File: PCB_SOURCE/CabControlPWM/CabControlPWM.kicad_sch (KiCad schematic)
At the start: 20 parts, among them J102 Jack-DC

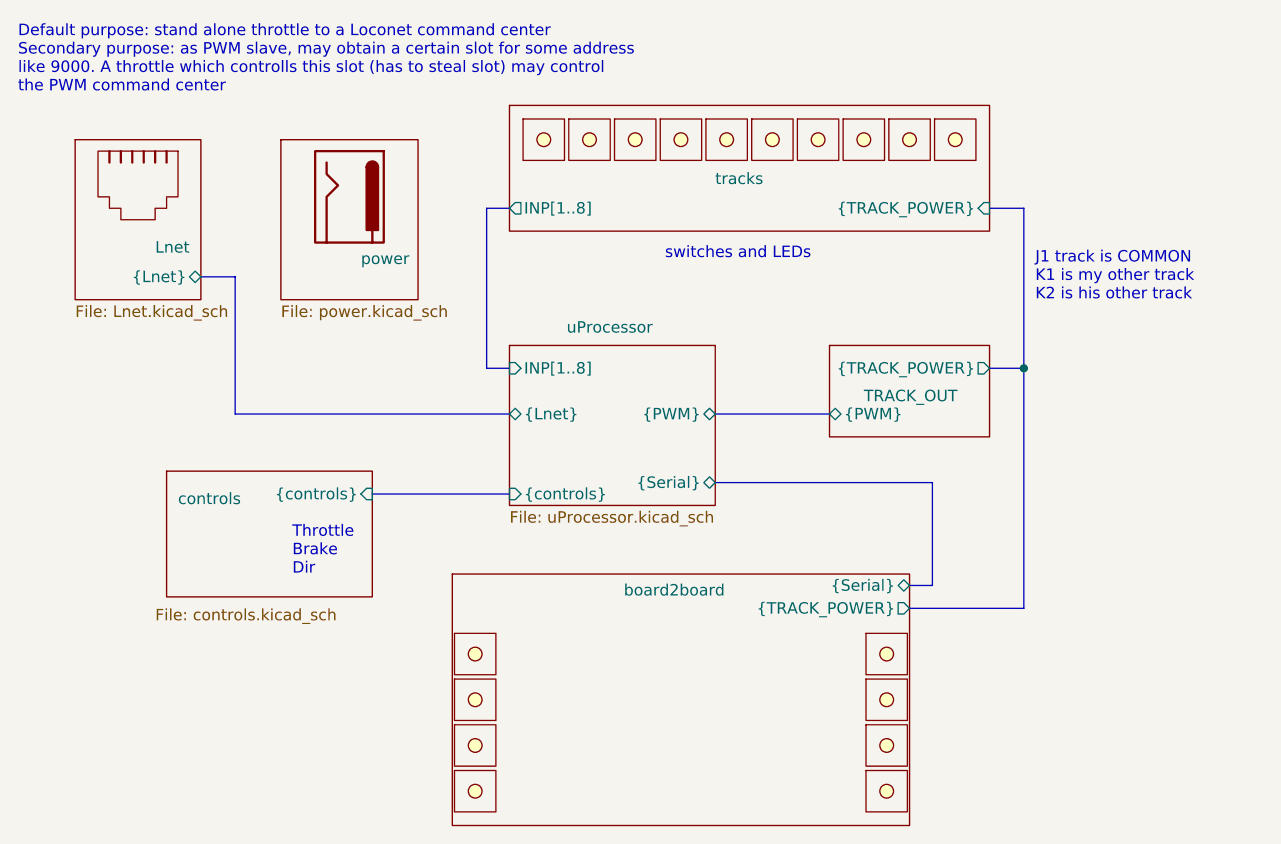
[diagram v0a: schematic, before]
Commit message: fixed bug in ahob program among others
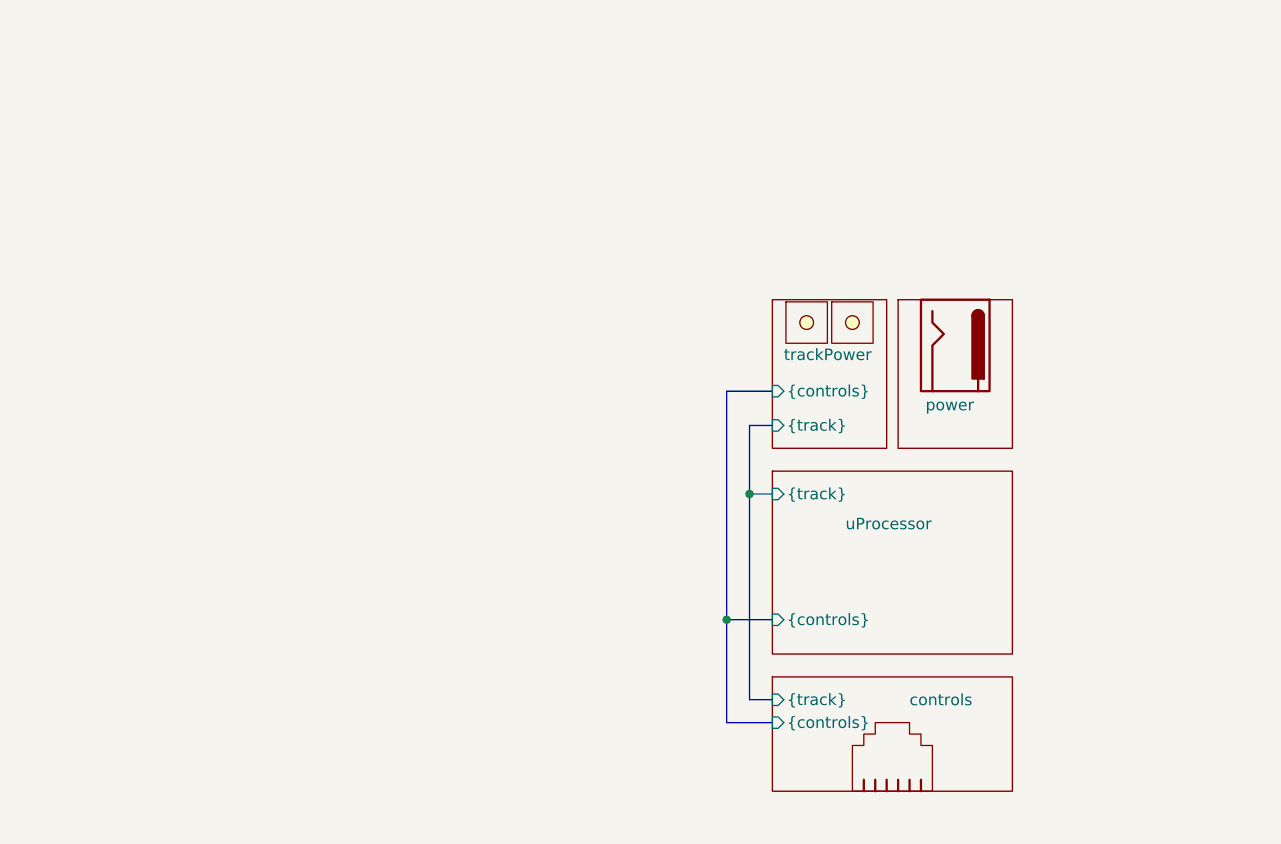
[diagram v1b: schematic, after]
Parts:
- removed u103, u104, u105, u106, u107, u108, u109, u110, u111, u112, u113, u114, u115, u116, u117, u118: ~, symbol custom_kicad_lib_sk:screwterminal
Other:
- removed sheet Lnet
- removed sheet TRACK_OUT
- removed sheet board2board
- removed sheet tracks
- added sheet trackPower (trackPower.kicad_sch)
- sheet controls ports: added {track}; removed none
- sheet uProcessor: file uProcessor.kicad_sch -> attiny85.kicad_sch
- sheet uProcessor ports: added {track}; removed INP[1..8], {Lnet}, {PWM}, {Serial}
- note removed: "Default purpose: stand alone throttle to a Loconet command center Secondary purpose: as PWM slave, may obtain a certain slot for some address like 9000. A throttle which controlls this slot (has to steal slot) may control the PWM command center"
- note removed: "J1 track is COMMON K1 is my other track K2 is his other track"
- note removed: "Throttle Brake Dir"
- note removed: "switches and LEDs"
